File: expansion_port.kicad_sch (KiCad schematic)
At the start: 3 parts, among them J1 Conn_01x02_Male, J2 Conn_01x02_Male, J3 Conn_02x30_Odd_Even

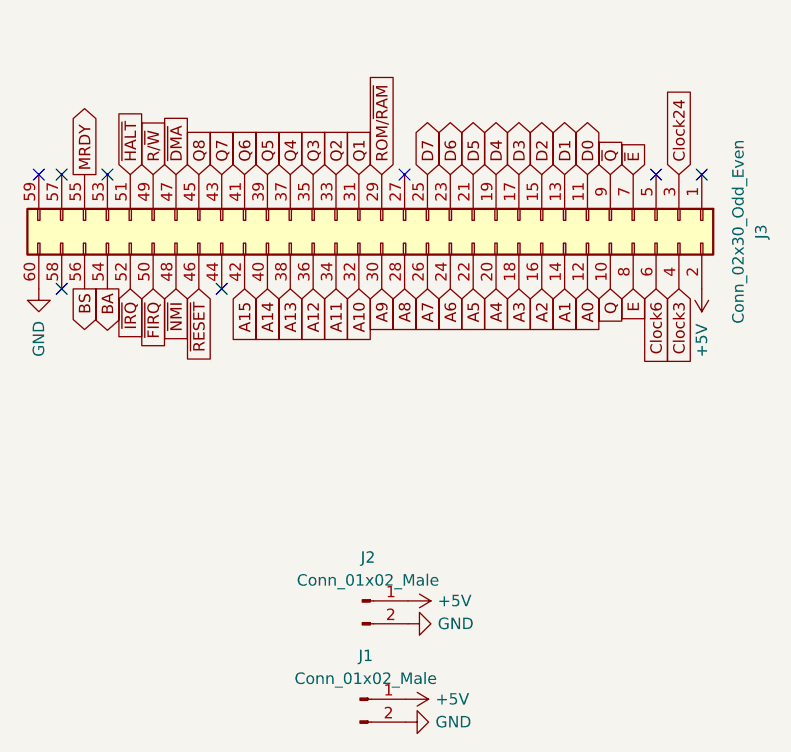
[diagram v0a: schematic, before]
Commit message: add mapped memory lane
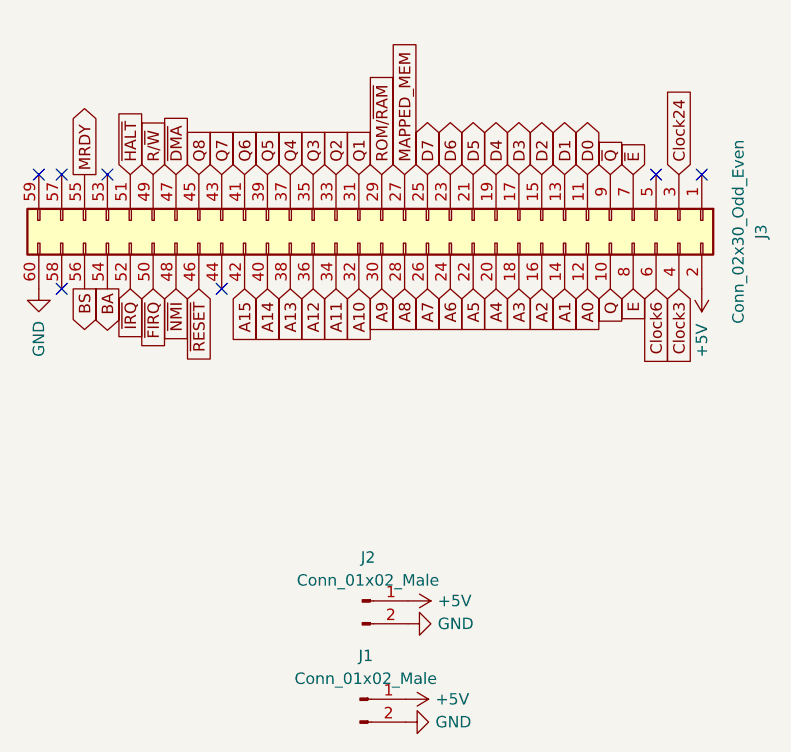
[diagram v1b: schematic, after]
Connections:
- net MAPPED_MEM: now reaches J3.27 (Pin_27)
- no-connect marks 8 -> 7
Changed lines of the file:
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@@
   (no_connect (at 102.362 58.547))
   (no_connect (at 176.022 58.547))
-  (no_connect (at 143.002 58.547))
   (no_connect (at 109.982 58.547))
   (no_connect (at 104.902 58.547))
@@
     )
   )
+  (global_label "MAPPED_MEM" (shape input) (at 143.002 58.547 90) (fields_autoplaced)
+    (effects (font (size 1.27 1.27)) (justify left))
+    (property "Intersheet References" "${INTERSHEET_REFS}" (id 0) (at 142.9226 43.6153 90)
+      (effects (font (size 1.27 1.27)) (justify left) hide)
+    )
+  )
